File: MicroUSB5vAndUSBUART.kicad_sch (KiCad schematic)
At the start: 21 parts, among them Q1 Q_NPN_BCE, Q2 Q_NPN_BCE, U2 USB_CON8, U3 CP2102N

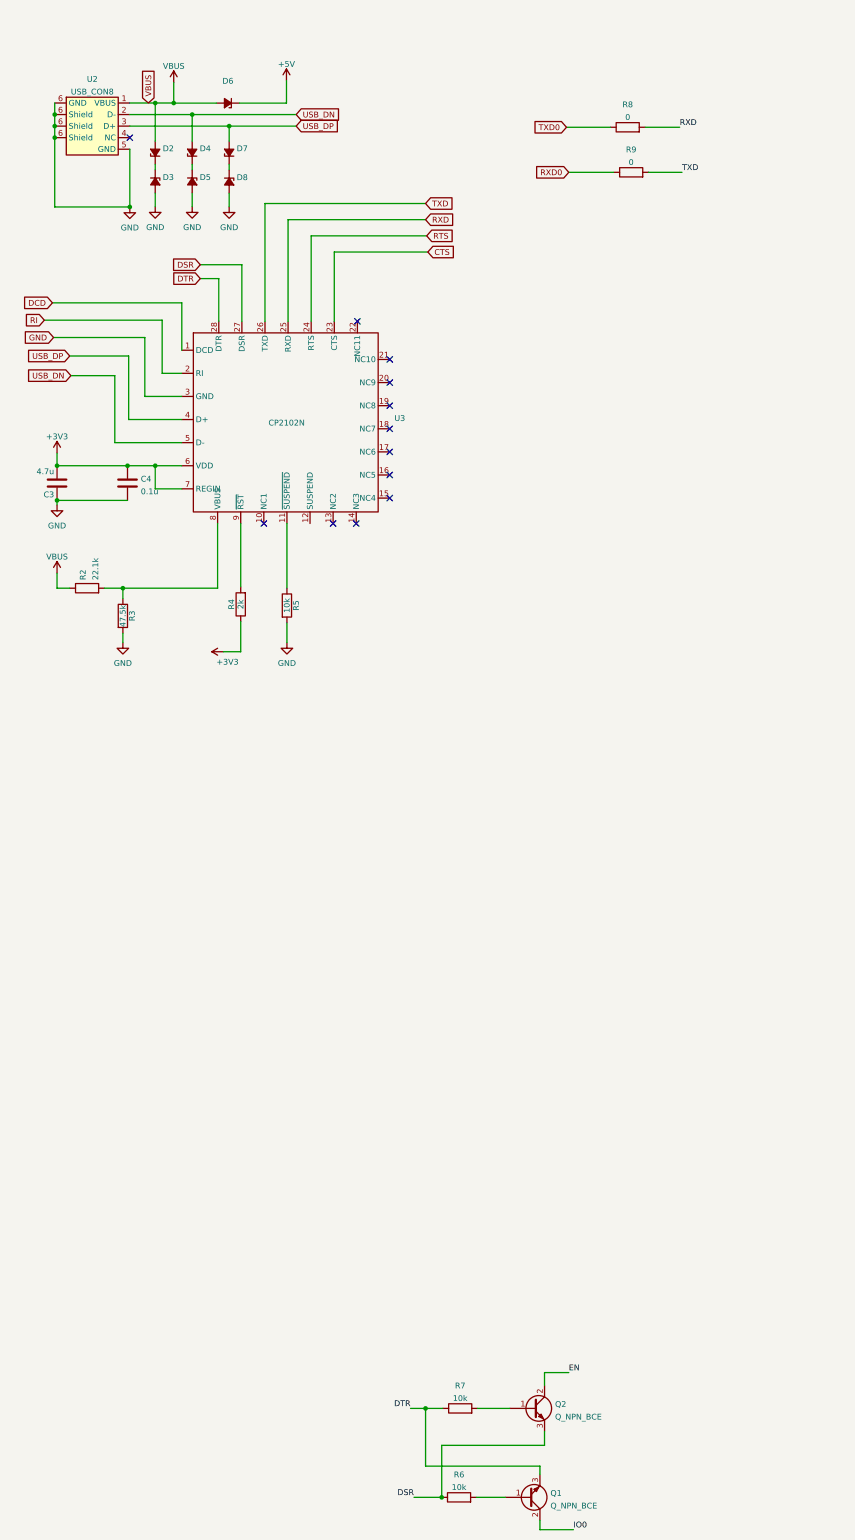
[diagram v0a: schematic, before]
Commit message: Routed most PCB traces
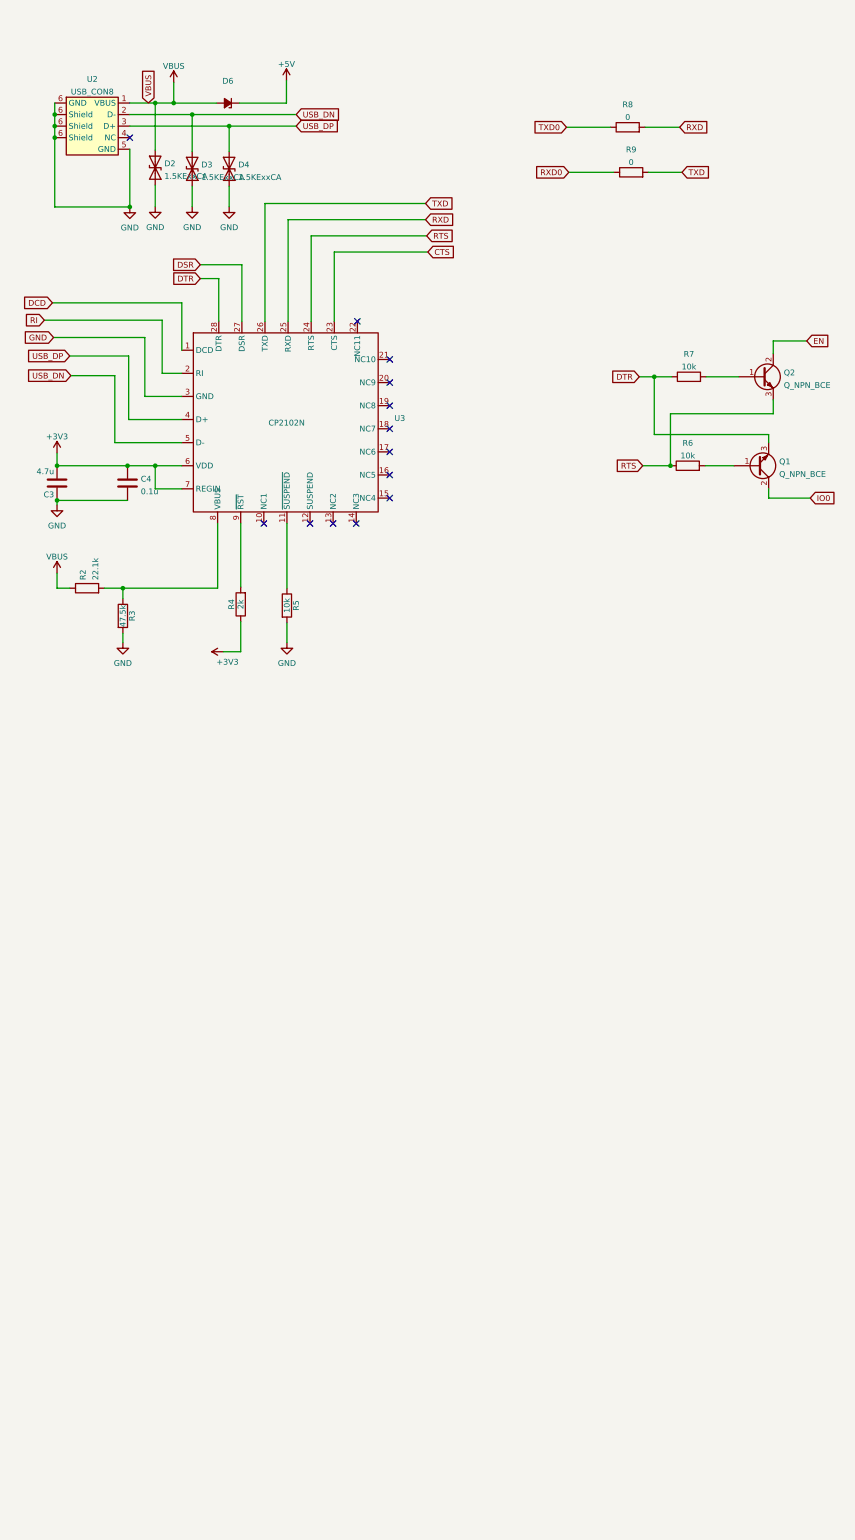
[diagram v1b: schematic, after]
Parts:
- removed D2, D3, D4, D5, D7, D8: D_Zener_Small_ALT, Diode_SMD:D_0603_1608Metric, symbol Device:D_Zener_Small_ALT
- added D2, D3, D4: 1.5KExxCA, Diode_SMD:D_0603_1608Metric_Pad1.05x0.95mm_HandSolder, symbol Diode:1.5KExxCA
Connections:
- net DSR: no longer Q2.3 (E), R6.1
- net GND: now also D2.1 (A1), D3.1 (A1), D4.1 (A1)
- net RTS: now also Q2.3 (E), R6.1
- net USB_DN: now also D3.2 (A2)
- net USB_DP: now also D4.2 (A2)
- net VBUS: now also D2.2 (A2)
- no-connect marks 12 -> 13
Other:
- moved on the sheet: Q1, Q2, R6, R7

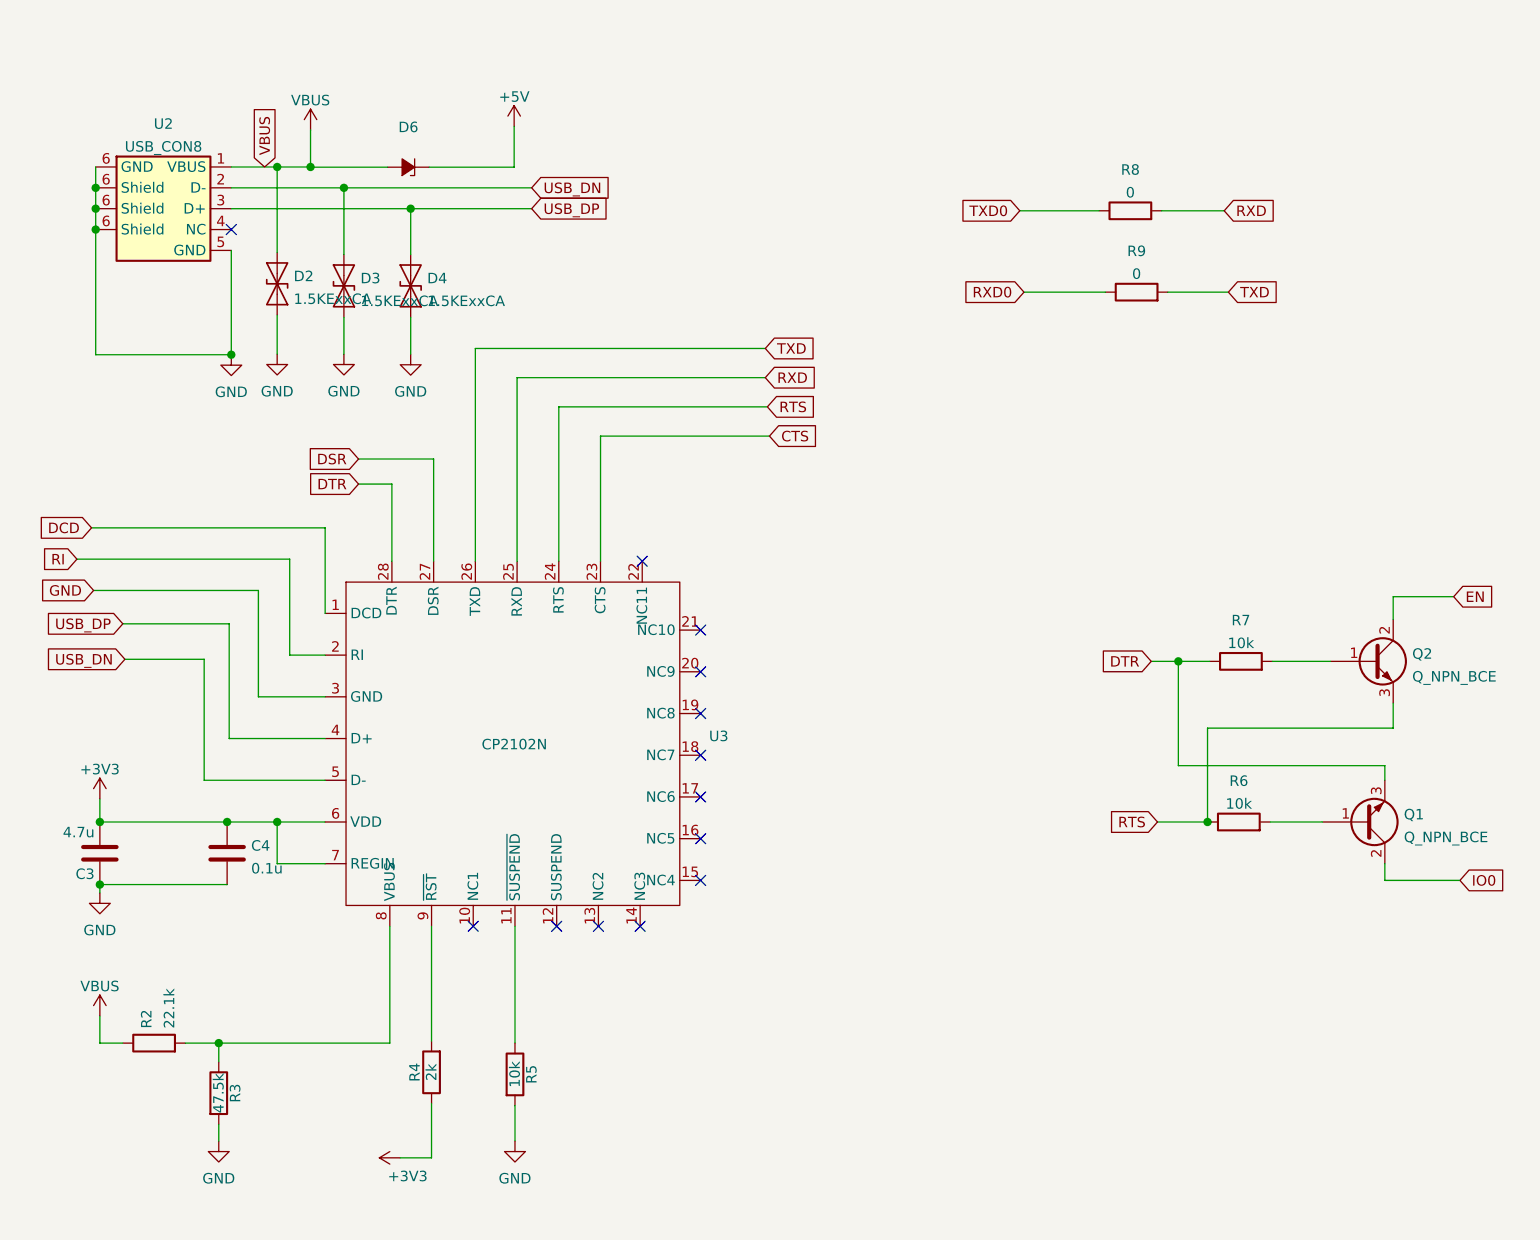
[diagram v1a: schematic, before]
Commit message: Added VOC and Optical Sensors
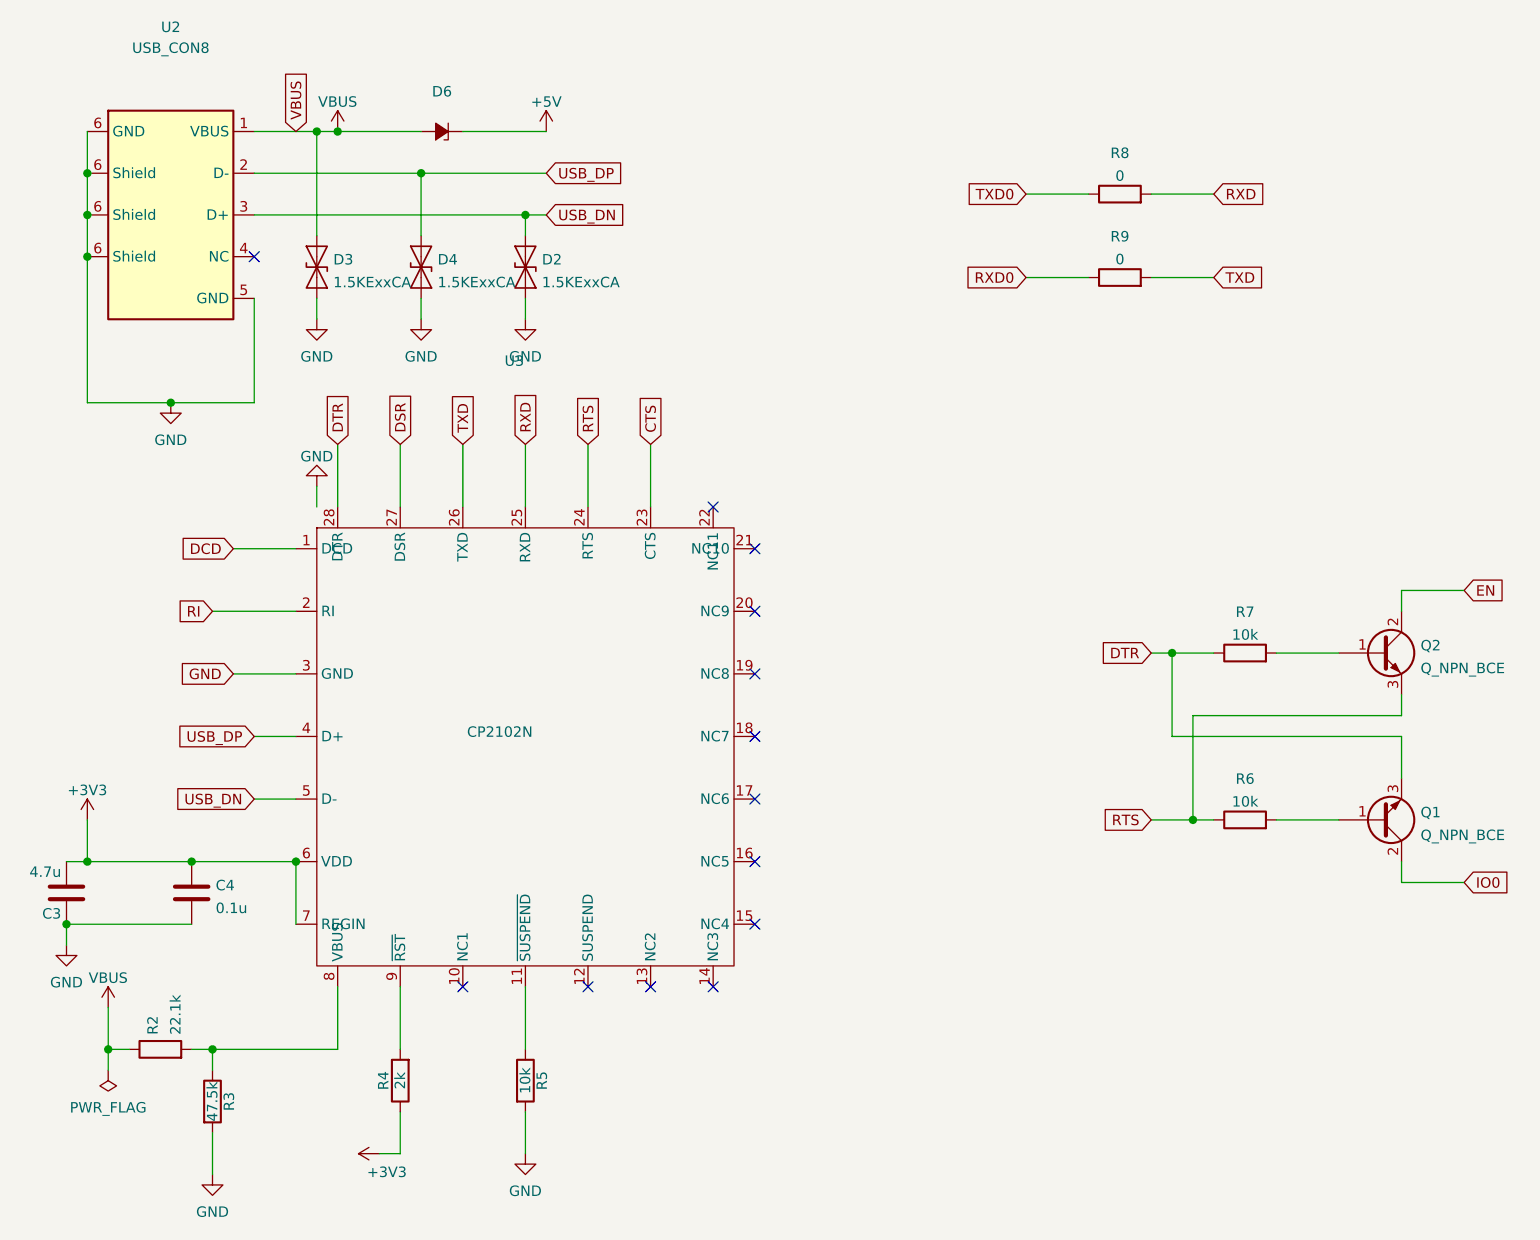
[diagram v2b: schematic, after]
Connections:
- net GND: now also U3.29 (GND)
- net USB_DN: now also D2.2 (A2), U2.3 (D+); no longer D3.2 (A2), U2.2 (D-)
- net USB_DP: now also U2.2 (D-); no longer U2.3 (D+)
- net VBUS: now also D3.2 (A2); no longer D2.2 (A2)
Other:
- moved on the sheet: C3, C4, D2, D3, D4, D6, Q1, Q2, R2, R3, R4, R5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
